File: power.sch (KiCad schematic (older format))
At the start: 41 parts

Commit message: I'm pretty happy with it now, will place tomorrow
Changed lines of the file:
@@
 $Descr A4 11693 8268
 encoding utf-8
-Sheet 4 4
+Sheet 3 4
 Title ""
 Date ""
@@
 Text HLabel 7750 3200 2    50   BiDi ~ 0
 SDA
-Text HLabel 8250 3300 2    50   Input ~ 0
+Text HLabel 8300 3300 2    50   Input ~ 0
 ~CE
+Wire Wire Line
+	8300 3300 8250 3300
+Connection ~ 8250 3300
 $EndSCHEMATC

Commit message: Add some part numbers, more changes
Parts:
- removed J?: Jack-DC, Connector_BarrelJack:BarrelJack_Horizontal, symbol Connector:Jack-DC
- added J301: BAT, Connector_PinSocket_2.54mm:PinSocket_1x02_P2.54mm_Vertical, symbol Connector_Generic:Conn_01x02
- C301: renamed from C?; JLC (none) -> 0805; LCSC (none) -> C49217; MPN (none) -> 0805F225M500NT
- C302, C309, C310, C316, C317: renamed from C?; JLC (none) -> 0603; LCSC (none) -> C14663; MPN (none) -> CC0603KRX7R9BB104
- C303: renamed from C?; JLC (none) -> 0805; LCSC (none) -> C45783; MPN (none) -> CL21A226MAQNNNE
- C306, C308, C311, C312, C313, C314, C315, C318, C319, C320, C321, C322: renamed from C?; footprint Capacitor_SMD:C_0805_2012Metric -> Capacitor_SMD:C_1206_3216Metric; JLC (none) -> 1206; LCSC (none) -> C13585; MPN (none) -> CL31A106KBHNNNE
- C307: renamed from C?; JLC (none) -> 0603; LCSC (none) -> C19666; MPN (none) -> CL10A475KO8NNNC
- J302: renamed from J?; footprint Automated:Conn_AMASS_XT60PW-F20 -> Connector_PinSocket_2.54mm:PinSocket_1x02_P2.54mm_Vertical
- R303: renamed from R?; JLC (none) -> 0603; LCSC (none) -> C22775; MPN (none) -> 0603WAF1000T5E
- R304, R307: renamed from R?; JLC (none) -> 0603; LCSC (none) -> C25804
- U301: renamed from U?; JLC (none) -> SOT-23-6L
- gave numbers to parts that had none: 15
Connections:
- net ACDRV2: now also J301.2 (Pin_2)
- net VAC2: now also J301.1 (Pin_1)

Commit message: Start with layout
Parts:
- added NT301: chonk, NetTie:NetTie-2_SMD_Pad2.0mm, symbol Device:Net-Tie_2
- added NT?: chonk_vbus, NetTie:NetTie-2_SMD_Pad2.0mm, symbol Device:Net-Tie_2
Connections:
- net VBUS: now also NT?.1; no longer C306.1, C308.1, C309.1, TP302.1, U302.2 (VBUSp), U302.3 (VBUSp)
- net VCC: now also NT301.1; no longer C317.1, C318.1, C319.1, C320.1, C321.1, C322.1, J303.1 (Pin_1), U302.25 (SYS)
- new net SYS: C317.1, C318.1, C319.1, C320.1, C321.1, C322.1, J303.1 (Pin_1), NT301.2, U302.25 (SYS)
- new net VBUSp: C306.1, C308.1, C309.1, NT?.2, TP302.1, U302.2 (VBUSp), U302.3 (VBUSp)
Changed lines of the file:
@@
 L power:VBUS #PWR0307
 U 1 1 5F1A365B
-P 6500 1850
-F 0 "#PWR0307" H 6500 1700 50  0001 C CNN
-F 1 "VBUS" H 6515 2023 50  0000 C CNN
-F 2 "" H 6500 1850 50  0001 C CNN
-F 3 "" H 6500 1850 50  0001 C CNN
-	1    6500 1850
-	1    0    0    -1
-$EndComp
-Wire Wire Line
-	6500 1850 6500 1950
+P 6500 1650
+F 0 "#PWR0307" H 6500 1500 50  0001 C CNN
+F 1 "VBUS" H 6515 1823 50  0000 C CNN
+F 2 "" H 6500 1650 50  0001 C CNN
+F 3 "" H 6500 1650 50  0001 C CNN
+	1    6500 1650
+	1    0    0    -1
+$EndComp
+Wire Wire Line
+	6500 1650 6500 1700
 $Comp
 L Device:L_Core_Ferrite L302
@@
 U 1 1 5F1A3708
 P 7100 2300
-F 0 "R303" H 7159 2346 50  0000 L CNN
-F 1 "100" H 7159 2255 50  0000 L CNN
+F 0 "R303" H 7042 2346 50  0000 R CNN
+F 1 "100" H 7042 2255 50  0000 R CNN
 F 2 "Resistor_SMD:R_0603_1608Metric" H 7100 2300 50  0001 C CNN
 F 3 "https://datasheet.lcsc.com/szlcsc/Uniroyal-Elec-0603WAF1000T5E_C22775.pdf" H 7100 2300 50  0001 C CNN
@@
 Wire Wire Line
 	7100 2400 7100 2550
-Wire Wire Line
-	7250 2550 7250 2500
-Wire Wire Line
-	7250 2500 7350 2500
-Wire Wire Line
-	7350 2500 7350 2050
-Connection ~ 7350 2050
-Wire Wire Line
-	7350 2050 7100 2050
+Connection ~ 7250 2050
+Wire Wire Line
+	7250 2050 7100 2050
 $Comp
 L power:GND #PWR0310
@@
 Connection ~ 7750 2050
 Wire Wire Line
-	7750 2050 7350 2050
+	7750 2050 7250 2050
 Text Label 8950 3000 0    50   ~ 0
 ILIM_HIZ
@@
 L power:VCC #PWR0316
 U 1 1 5F1A378B
-P 9100 3900
-F 0 "#PWR0316" H 9100 3750 50  0001 C CNN
-F 1 "VCC" H 9115 4073 50  0000 C CNN
-F 2 "" H 9100 3900 50  0001 C CNN
-F 3 "" H 9100 3900 50  0001 C CNN
-	1    9100 3900
+P 9100 3650
+F 0 "#PWR0316" H 9100 3500 50  0001 C CNN
+F 1 "VCC" H 9115 3823 50  0000 C CNN
+F 2 "" H 9100 3650 50  0001 C CNN
+F 3 "" H 9100 3650 50  0001 C CNN
+	1    9100 3650
 	1    0    0    -1
 $EndComp
@@
 Wire Wire Line
 	4450 6000 4800 6000
+$Comp
+L Device:Net-Tie_2 NT301
+U 1 1 5F0DC79C
+P 9100 3800
+F 0 "NT301" V 9100 3844 50  0000 L CNN
+F 1 "chonk" V 9145 3844 50  0001 L CNN
+F 2 "NetTie:NetTie-2_SMD_Pad2.0mm" H 9100 3800 50  0001 C CNN
+F 3 "~" H 9100 3800 50  0001 C CNN
+	1    9100 3800
+	0    1    1    0
+$EndComp
+Wire Wire Line
+	9100 3700 9100 3650
+Text Label 7900 4000 0    50   ~ 0
+SYS
+$Comp
+L Device:Net-Tie_2 NT?
+U 1 1 5F0F4068
+P 6500 1800
+F 0 "NT?" V 6500 1844 50  0000 L CNN
+F 1 "chonk_vbus" V 6545 1844 50  0001 L CNN
+F 2 "NetTie:NetTie-2_SMD_Pad2.0mm" H 6500 1800 50  0001 C CNN
+F 3 "~" H 6500 1800 50  0001 C CNN
+	1    6500 1800
+	0    1    1    0
+$EndComp
+Wire Wire Line
+	6500 1900 6500 1950
+Text Label 6500 2150 3    50   ~ 0
+VBUS_BQ
+Wire Wire Line
+	7250 2050 7250 2550
 $EndSCHEMATC

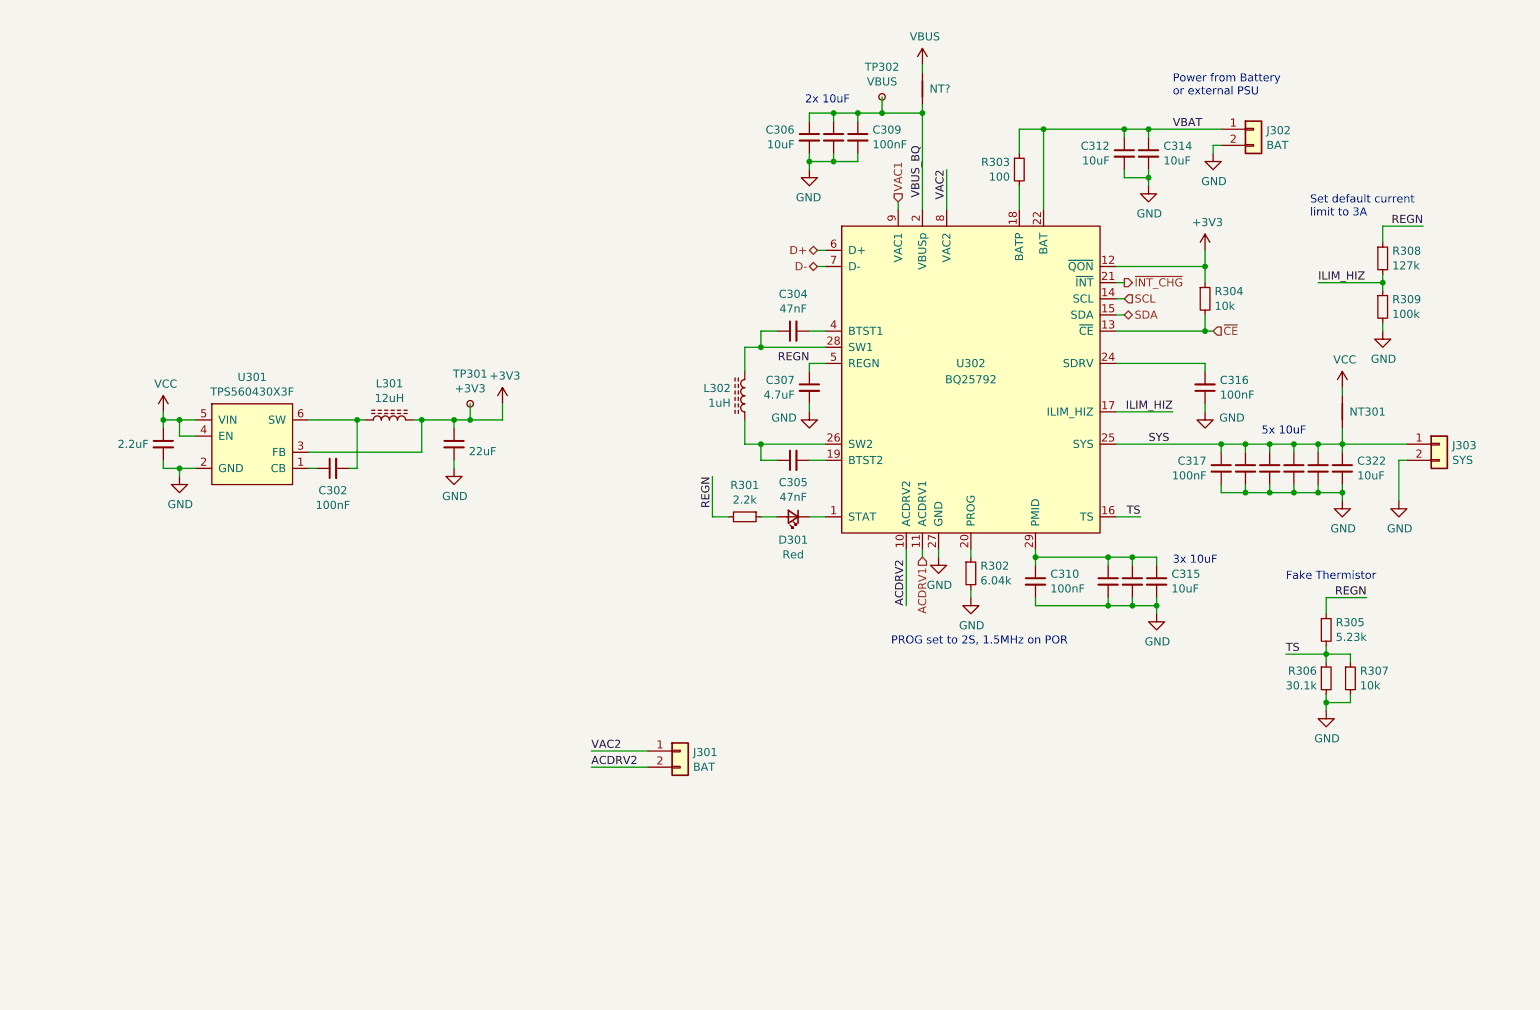
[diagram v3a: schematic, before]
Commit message: placed to 50x50mm, started to route
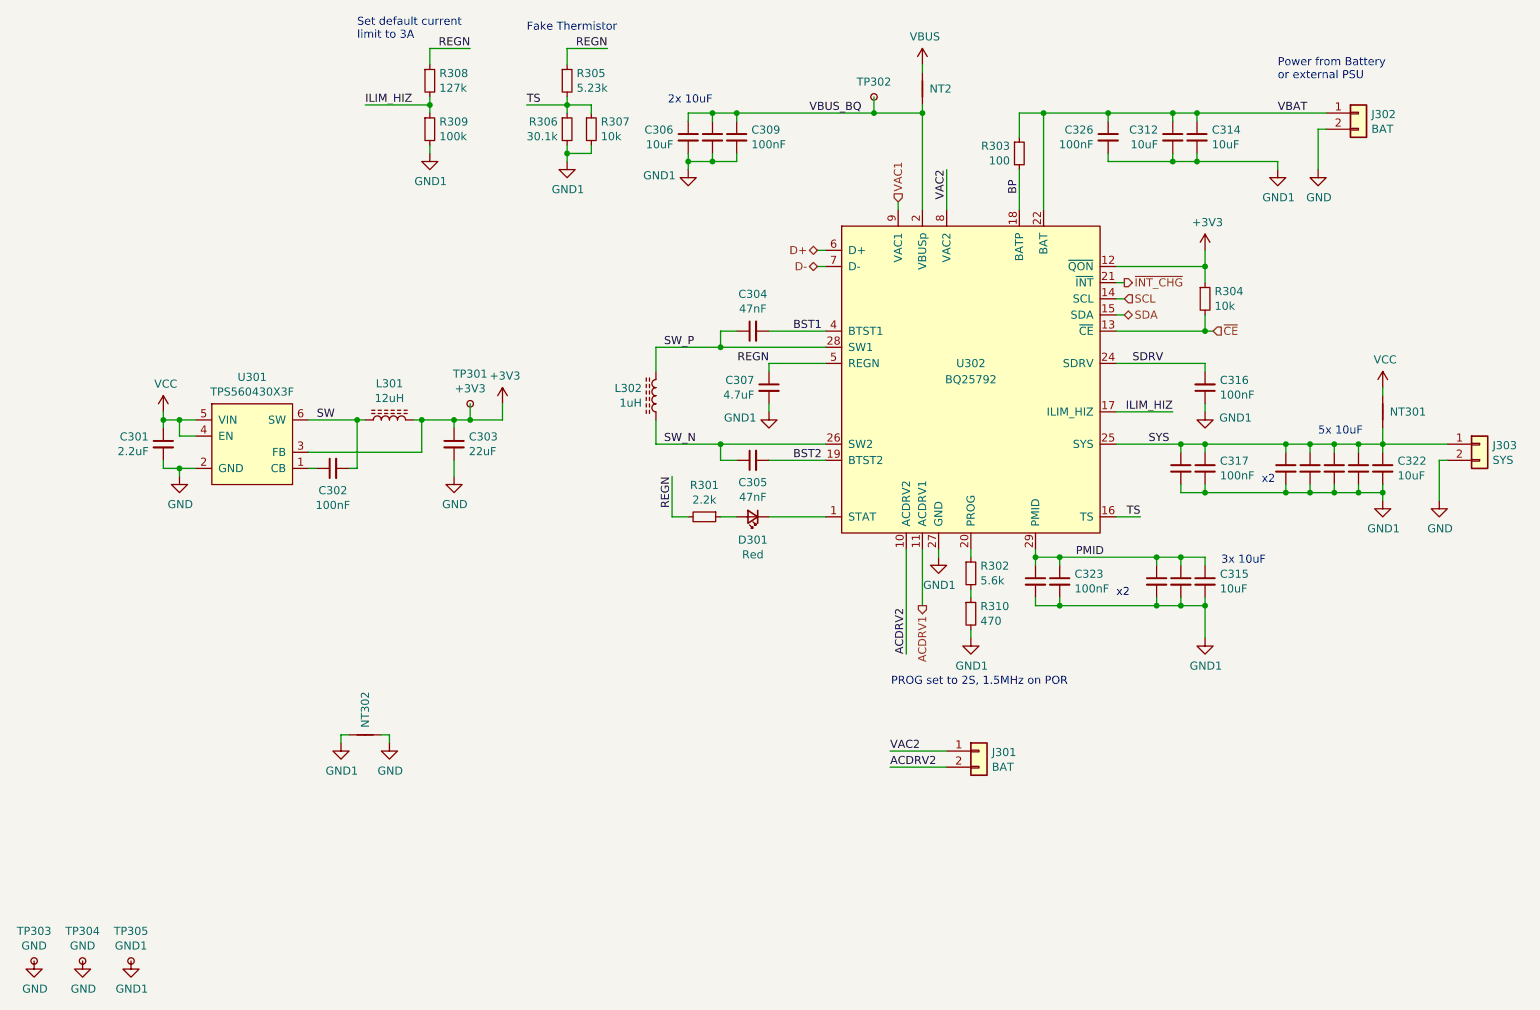
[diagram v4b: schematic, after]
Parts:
- added C323, C324, C326: 100nF, Capacitor_SMD:C_0402_1005Metric, symbol Device:C_Small
- added NT302: chonk, NetTie:NetTie-2_SMD_Pad2.0mm, symbol Device:Net-Tie_2
- added R310: 470, Resistor_SMD:R_0402_1005Metric, symbol Device:R_Small
- added TP303, TP304: GND, TestPoint:TestPoint_THTPad_D2.0mm_Drill1.0mm, symbol Connector:TestPoint_Small
- added TP305: GND1, TestPoint:TestPoint_THTPad_D2.0mm_Drill1.0mm, symbol Connector:TestPoint_Small
- C309: footprint Capacitor_SMD:C_0603_1608Metric -> Capacitor_SMD:C_0402_1005Metric; JLC 0603 -> 0402; LCSC C14663 -> (none); MPN CC0603KRX7R9BB104 -> (none)
- C310, C316, C317: footprint Capacitor_SMD:C_0603_1608Metric -> Capacitor_SMD:C_0402_1005Metric; JLC 0603 -> (none); LCSC C14663 -> (none); MPN CC0603KRX7R9BB104 -> (none)
- R302: value 6.04k -> 5.6k; footprint Resistor_SMD:R_0603_1608Metric -> Resistor_SMD:R_0402_1005Metric
- TP302: value VBUS -> VBUS_BQ
- gave numbers to parts that had none: 1
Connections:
- net GND: now also NT302.2, TP303.1, TP304.1; no longer C306.2, C307.2, C308.2, C309.2, C310.2, C311.2, C312.2, C313.2, C314.2, C315.2, C316.1, C317.2, C318.2, C319.2, C320.2, C321.2, C322.2, R302.2, R306.2, R307.2, R309.2, U302.27 (GND)
- net SYS: now also C324.1
- net VBAT: now also C326.1
- net BP: now reaches R303.2, U302.18 (BATP)
- net BST2: now reaches C305.2, U302.19 (BTST2)
- net SDRV: now reaches C316.2, U302.24 (SDRV)
- net SW_N: now reaches C305.1, L302.1, U302.26 (SW2)
- net SW_P: now reaches C304.1, L302.2, U302.28 (SW1)
- net PMID: now reaches C310.1, C311.1, C313.1, C315.1, U302.29 (PMID)
- net PMID: now also C323.1
- net BST1: now reaches C304.2, U302.4 (BTST1)
- net SW: now reaches C302.2, L301.1, U301.6 (SW)
- new net: R302.2, R310.1
- new net GND1: C306.2, C307.2, C308.2, C309.2, C310.2, C311.2, C312.2, C313.2, C314.2, C315.2, C316.1, C317.2, C318.2, C319.2, C320.2, C321.2, C322.2, C323.2, C324.2, C326.2, NT302.1, R306.2, R307.2, R309.2, R310.2, TP305.1, U302.27 (GND)
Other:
- note added: "x2"
- moved on the sheet: C304, C305, C306, C307, C312, C314, C315, C317, C322, D301, J301, J302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

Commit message: partially routed
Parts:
- C310, C317, C323, C324: footprint Capacitor_SMD:C_0402_1005Metric -> Capacitor_SMD:C_0603_1608Metric
- NT301: footprint NetTie:NetTie-2_SMD_Pad2.0mm -> NetTie:NetTie-2_SMD_Pad0.5mm
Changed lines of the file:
@@
 F 0 "C310" H 7292 4896 50  0001 L CNN
 F 1 "100nF" H 7292 4805 50  0001 L CNN
-F 2 "Capacitor_SMD:C_0402_1005Metric" H 7200 4850 50  0001 C CNN
+F 2 "Capacitor_SMD:C_0603_1608Metric" H 7200 4850 50  0001 C CNN
 F 3 "~" H 7200 4850 50  0001 C CNN
 F 4 "" H 7200 4850 50  0001 C CNN "JLC"
@@
 F 0 "C317" H 8342 4196 50  0000 L CNN
 F 1 "100nF" H 8342 4105 50  0000 L CNN
-F 2 "Capacitor_SMD:C_0402_1005Metric" H 8250 4150 50  0001 C CNN
+F 2 "Capacitor_SMD:C_0603_1608Metric" H 8250 4150 50  0001 C CNN
 F 3 "~" H 8250 4150 50  0001 C CNN
 F 4 "" H 8250 4150 50  0001 C CNN "JLC"
@@
 F 0 "NT301" V 9350 3844 50  0000 L CNN
 F 1 "chonk" V 9395 3844 50  0001 L CNN
-F 2 "NetTie:NetTie-2_SMD_Pad2.0mm" H 9350 3800 50  0001 C CNN
+F 2 "NetTie:NetTie-2_SMD_Pad0.5mm" H 9350 3800 50  0001 C CNN
 F 3 "~" H 9350 3800 50  0001 C CNN
 	1    9350 3800
@@
 F 0 "C324" H 8009 4196 50  0001 R CNN
 F 1 "100nF" H 8009 4105 50  0001 R CNN
-F 2 "Capacitor_SMD:C_0402_1005Metric" H 8100 4150 50  0001 C CNN
+F 2 "Capacitor_SMD:C_0603_1608Metric" H 8100 4150 50  0001 C CNN
 F 3 "~" H 8100 4150 50  0001 C CNN
 F 4 "" H 8100 4150 50  0001 C CNN "JLC"
@@
 F 0 "C323" H 7442 4896 50  0000 L CNN
 F 1 "100nF" H 7442 4805 50  0000 L CNN
-F 2 "Capacitor_SMD:C_0402_1005Metric" H 7350 4850 50  0001 C CNN
+F 2 "Capacitor_SMD:C_0603_1608Metric" H 7350 4850 50  0001 C CNN
 F 3 "~" H 7350 4850 50  0001 C CNN
 F 4 "" H 7350 4850 50  0001 C CNN "JLC"

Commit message: Add a few more PNs, change D401 to a standard part
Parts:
- R301: JLC (none) -> 0603; LCSC (none) -> C4190; MPN (none) -> 0603WAF2201T5E
- R302: JLC (none) -> 0603; LCSC (none) -> C23189
- R309: JLC (none) -> 0603; LCSC (none) -> C25803
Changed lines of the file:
@@
 F 2 "Resistor_SMD:R_0402_1005Metric" H 6800 4800 50  0001 C CNN
 F 3 "~" H 6800 4800 50  0001 C CNN
+F 4 "0603" H 6800 4800 50  0001 C CNN "JLC"
+F 5 "C23189" H 6800 4800 50  0001 C CNN "LCSC"
 	1    6800 4800
 	1    0    0    -1
@@
 F 2 "Resistor_SMD:R_0603_1608Metric" H 3450 2050 50  0001 C CNN
 F 3 "~" H 3450 2050 50  0001 C CNN
+F 4 "0603" H 3450 2050 50  0001 C CNN "JLC"
+F 5 "C25803" H 3450 2050 50  0001 C CNN "LCSC"
 	1    3450 2050
 	1    0    0    -1
@@
 F 2 "Resistor_SMD:R_0603_1608Metric" H 5150 4450 50  0001 C CNN
 F 3 "~" H 5150 4450 50  0001 C CNN
+F 4 "0603" V 5150 4450 50  0001 C CNN "JLC"
+F 5 "C4190" V 5150 4450 50  0001 C CNN "LCSC"
+F 6 "0603WAF2201T5E" V 5150 4450 50  0001 C CNN "MPN"
 	1    5150 4450
 	0    1    1    0

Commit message: finished routing. no silk artwork.
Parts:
- renumbered C306 to C304, C308 to C305, C309 to C306, C304 to C307, C305 to C308, C307 to C309, C323 to C311, C326 to C312, C311 to C313, C312 to C314, C324 to C315, C313 to C316, C314 to C317, C316 to C318, C317 to C319, C315 to C320, C318 to C321, C319 to C322, C320 to C323, C321 to C324, C322 to C325, J303 to J304, NT302 to NT301, NT2 to NT302, NT301 to NT303, R308 to R301, R309 to R302, R305 to R303, R306 to R304, R307 to R305, R301 to R306, R302 to R307, R310 to R308, R303 to R309, R304 to R310, TP303 to TP301, TP304 to TP302, TP305 to TP303, TP301 to TP304, TP302 to TP305

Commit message: Add a few more parts, fix PCB origin problem
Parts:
- R308: JLC (none) -> 0402; LCSC (none) -> C25117
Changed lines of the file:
@@
 F 2 "Resistor_SMD:R_0402_1005Metric" H 6800 5050 50  0001 C CNN
 F 3 "~" H 6800 5050 50  0001 C CNN
+F 4 "C25117" H 6800 5050 50  0001 C CNN "LCSC"
+F 5 "0402" H 6800 5050 50  0001 C CNN "JLC"
 	1    6800 5050
 	1    0    0    -1
